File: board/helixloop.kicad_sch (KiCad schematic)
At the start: 2 parts, among them J1 Conn_01x04, J2 Conn_01x02

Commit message: finally get pixels all aligned right by laying out the sine-wave in chunks and using different pixel spacing for outer vs inner curve
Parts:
- added C1, C2: 10uF, Capacitor_SMD:C_0402_1005Metric, symbol Device:C
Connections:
- net +5V: now also C1.2, C2.2
- net GND: now also C1.1, C2.1
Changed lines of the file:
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@@
   (junction (at 116.205 48.895) (diameter 0) (color 0 0 0 0)
   )
+  (junction (at 154.305 37.465) (diameter 0) (color 0 0 0 0)
+  )
   (junction (at 154.305 29.21) (diameter 0) (color 0 0 0 0)
   )
   (junction (at 90.17 48.895) (diameter 0) (color 0 0 0 0)
   )
+  (junction (at 50.165 34.925) (diameter 0) (color 0 0 0 0)
+  )
+  (junction (at 57.785 42.545) (diameter 0) (color 0 0 0 0)
+  )
   (junction (at 154.305 48.895) (diameter 0) (color 0 0 0 0)
   )
@@
   )
   (junction (at 62.865 42.545) (diameter 0) (color 0 0 0 0)
+  )
+  (junction (at 154.305 40.005) (diameter 0) (color 0 0 0 0)
   )
   (no_connect (at 141.605 37.465))
   (no_connect (at 141.605 40.005))
-  (wire (pts (xy 45.72 42.545) (xy 62.865 42.545))
+  (wire (pts (xy 45.72 42.545) (xy 57.785 42.545))
     (stroke (width 0) (type default) (color 0 0 0 0))
   )
@@
     (stroke (width 0) (type default) (color 0 0 0 0))
   )
+  (wire (pts (xy 153.035 40.005) (xy 153.035 42.545))
+    (stroke (width 0) (type default) (color 0 0 0 0))
+  )
   (wire (pts (xy 140.335 37.465) (xy 141.605 37.465))
     (stroke (width 0) (type default) (color 0 0 0 0))
   )
+  (wire (pts (xy 57.785 42.545) (xy 62.865 42.545))
+    (stroke (width 0) (type default) (color 0 0 0 0))
+  )
   (wire (pts (xy 45.72 37.465) (xy 66.04 37.465))
     (stroke (width 0) (type default) (color 0 0 0 0))
@@
     (stroke (width 0) (type default) (color 0 0 0 0))
   )
+  (wire (pts (xy 153.035 37.465) (xy 153.035 34.925))
+    (stroke (width 0) (type default) (color 0 0 0 0))
+  )
   (wire (pts (xy 90.17 42.545) (xy 92.075 42.545))
     (stroke (width 0) (type default) (color 0 0 0 0))
@@
     (stroke (width 0) (type default) (color 0 0 0 0))
   )
+  (wire (pts (xy 153.035 34.925) (xy 149.225 34.925))
+    (stroke (width 0) (type default) (color 0 0 0 0))
+  )
+  (wire (pts (xy 153.035 42.545) (xy 149.225 42.545))
+    (stroke (width 0) (type default) (color 0 0 0 0))
+  )
   (wire (pts (xy 90.17 29.21) (xy 90.17 34.925))
     (stroke (width 0) (type default) (color 0 0 0 0))
@@
     (stroke (width 0) (type default) (color 0 0 0 0))
   )
-  (wire (pts (xy 45.72 34.925) (xy 62.865 34.925))
+  (wire (pts (xy 45.72 34.925) (xy 50.165 34.925))
     (stroke (width 0) (type default) (color 0 0 0 0))
   )
@@
     (stroke (width 0) (type default) (color 0 0 0 0))
   )
+  (wire (pts (xy 50.165 34.925) (xy 62.865 34.925))
+    (stroke (width 0) (type default) (color 0 0 0 0))
+  )
   (wire (pts (xy 116.205 29.21) (xy 154.305 29.21))
     (stroke (width 0) (type default) (color 0 0 0 0))
   )
+  (wire (pts (xy 154.305 40.005) (xy 153.035 40.005))
+    (stroke (width 0) (type default) (color 0 0 0 0))
+  )
+  (wire (pts (xy 50.165 30.48) (xy 50.165 34.925))
+    (stroke (width 0) (type default) (color 0 0 0 0))
+  )
+  (wire (pts (xy 57.785 30.48) (xy 57.785 42.545))
+    (stroke (width 0) (type default) (color 0 0 0 0))
+  )
   (wire (pts (xy 88.265 40.005) (xy 92.075 40.005))
+    (stroke (width 0) (type default) (color 0 0 0 0))
+  )
+  (wire (pts (xy 154.305 37.465) (xy 153.035 37.465))
     (stroke (width 0) (type default) (color 0 0 0 0))
   )
@@
     )
     (pin "1")
+  )
+  (symbol (lib_id "Device:C") (at 53.975 30.48 90) (unit 1)
+    (in_bom yes) (on_board yes) (fields_autoplaced)
+    (property "Reference" "C1" (id 0) (at 53.975 24.6212 90))
+    (property "Value" "10uF" (id 1) (at 53.975 27.1581 90))
+    (property "Footprint" "Capacitor_SMD:C_0402_1005Metric" (id 2) (at 57.785 29.5148 0)
+      (effects (font (size 1.27 1.27)) hide)
+    )
+    (property "Datasheet" "~" (id 3) (at 53.975 30.48 0)
+      (effects (font (size 1.27 1.27)) hide)
+    )
+    (pin "1")
+    (pin "2")
+  )
+  (symbol (lib_id "Device:C") (at 149.225 38.735 0) (unit 1)
+    (in_bom yes) (on_board yes)
+    (property "Reference" "C2" (id 0) (at 147.955 33.02 0)
+      (effects (font (size 1.27 1.27)) (justify left))
+    )
+    (property "Value" "10uF" (id 1) (at 146.685 44.45 0)
+      (effects (font (size 1.27 1.27)) (justify left))
+    )
+    (property "Footprint" "Capacitor_SMD:C_0402_1005Metric" (id 2) (at 150.1902 42.545 0)
+      (effects (font (size 1.27 1.27)) hide)
+    )
+    (property "Datasheet" "~" (id 3) (at 149.225 38.735 0)
+      (effects (font (size 1.27 1.27)) hide)
+    )
+    (pin "1")
+    (pin "2")
   )
   (symbol (lib_id "power:+5V") (at 154.305 48.895 180) (unit 1)
@@
       (reference "#PWR0110") (unit 1) (value "+5V") (footprint "")
     )
+    (path "/be7e036f-0d5d-4156-a7b8-31f688740589"
+      (reference "C1") (unit 1) (value "10uF") (footprint "Capacitor_SMD:C_0402_1005Metric")
+    )
+    (path "/cb59f15f-90e9-4305-b7cf-ed2b3c2ebbf8"
+      (reference "C2") (unit 1) (value "10uF") (footprint "Capacitor_SMD:C_0402_1005Metric")
+    )
     (path "/b7ef0c2d-d029-4ee4-8532-c6efa483cf4c/e5639c70-98d2-40ea-b831-829e12089cc3"

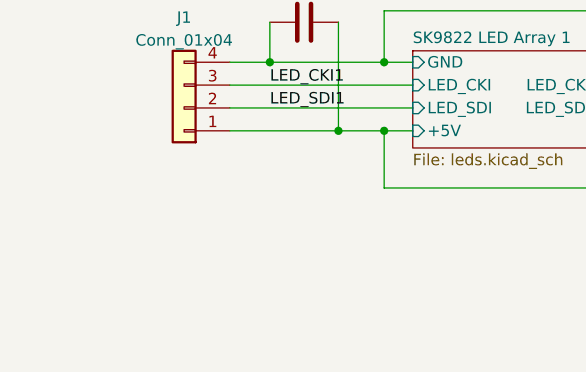
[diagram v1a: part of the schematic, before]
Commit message: add some labels to the back
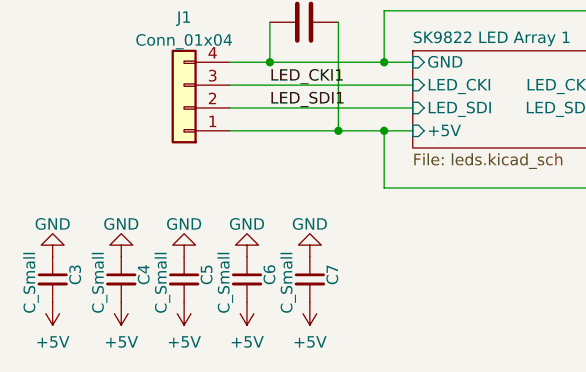
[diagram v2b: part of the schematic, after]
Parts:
- added C3, C4, C5, C6, C7: C_Small, Capacitor_SMD:C_0402_1005Metric, symbol Device:C_Small
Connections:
- net +5V: now also C3.2, C4.2, C5.2, C6.2, C7.2
- net GND: now also C3.1, C4.1, C5.1, C6.1, C7.1

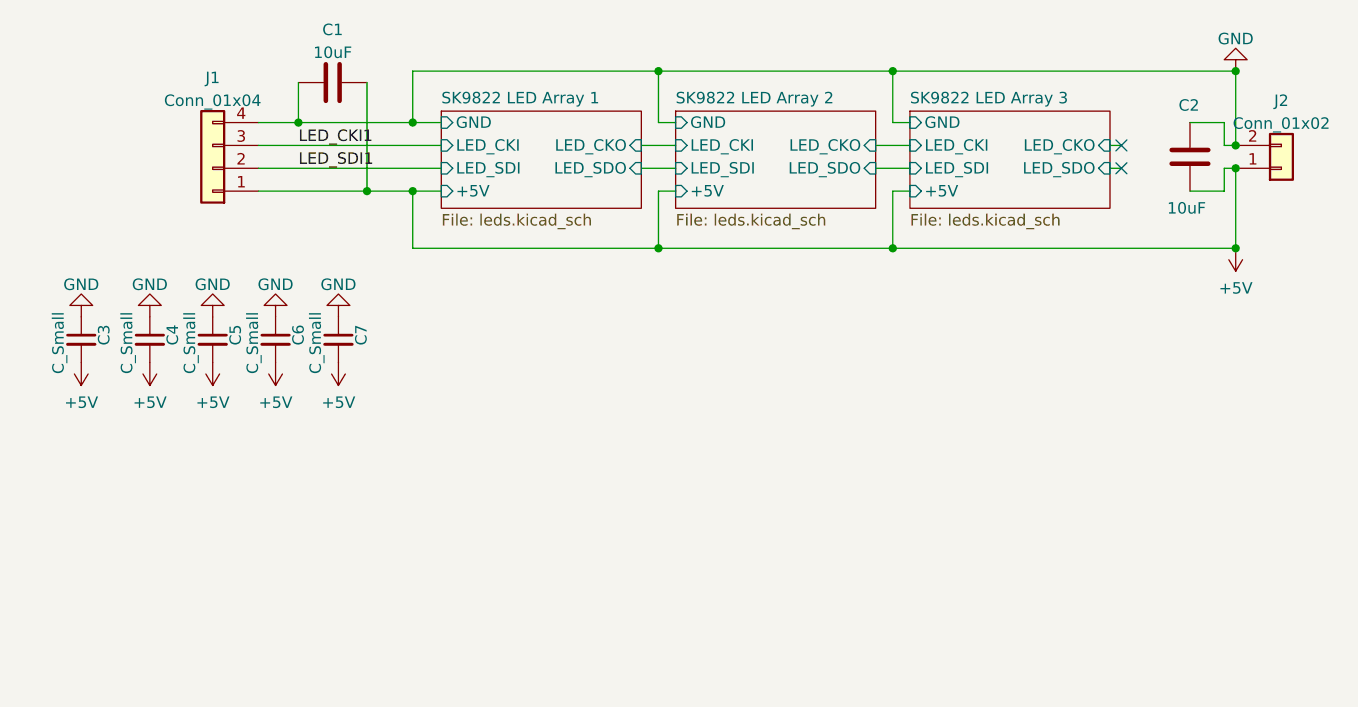
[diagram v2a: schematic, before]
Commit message: fix the SK9822-EC20 footprint, which wasn't to spec for some reason? sprinkle in capacitors in a more decorative arrangement; add a mounting hole in the center; fix all ERC errors
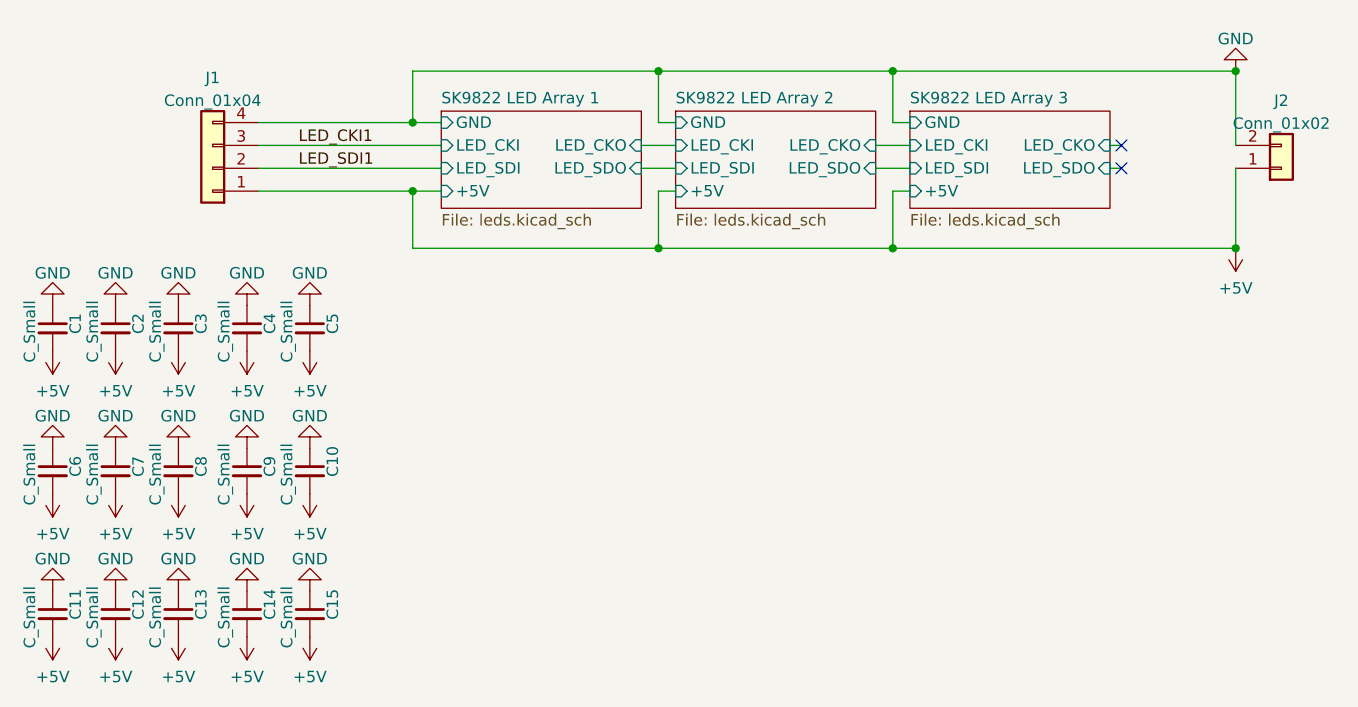
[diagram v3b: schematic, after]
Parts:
- removed C1, C2: 10uF, Capacitor_SMD:C_0402_1005Metric, symbol Device:C
- added C1, C10, C11, C12, C13, C14, C15, C2, C8, C9: C_Small, Capacitor_SMD:C_0402_1005Metric, symbol Device:C_Small
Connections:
- net +5V: now also C1.2, C10.2, C11.2, C12.2, C13.2, C14.2, C15.2, C2.2, C8.2, C9.2
- net GND: now also C1.1, C10.1, C11.1, C12.1, C13.1, C14.1, C15.1, C2.1, C8.1, C9.1
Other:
- moved on the sheet: C3, C4, C5

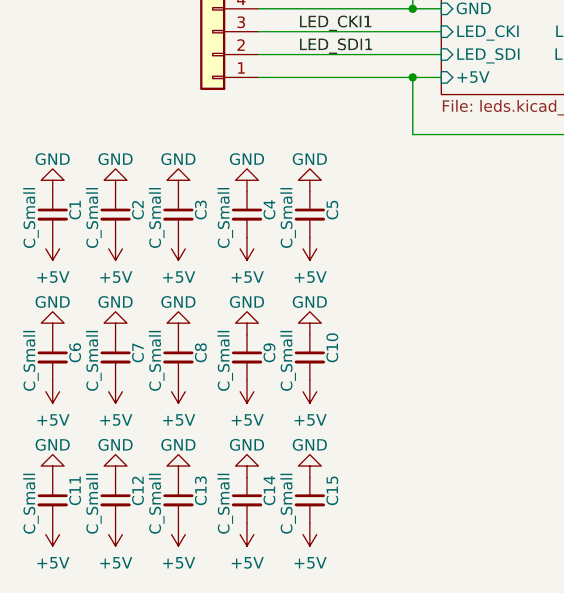
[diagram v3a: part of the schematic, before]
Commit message: annotate capacitors as 10uF
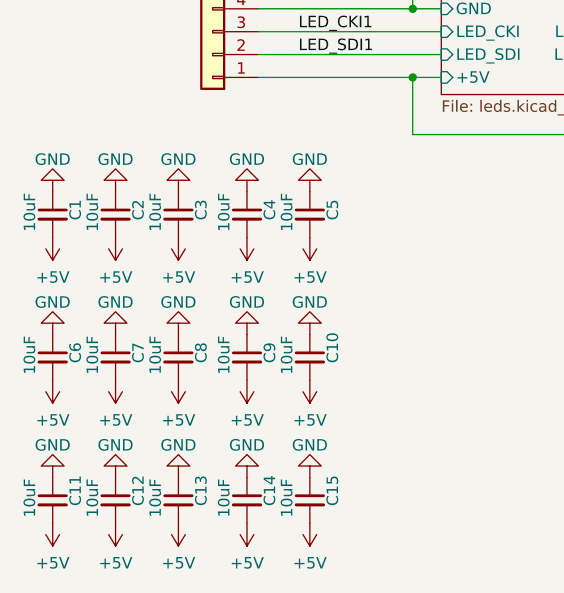
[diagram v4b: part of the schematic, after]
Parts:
- C1, C10, C11, C12, C13, C14, C15, C2, C3, C4, C5, C6, C7, C8, C9: value C_Small -> 10uF
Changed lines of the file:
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@@
       (effects (font (size 1.27 1.27)) (justify left))
     )
-    (property "Value" "C_Small" (id 1) (at 41.91 61.595 90)
+    (property "Value" "10uF" (id 1) (at 41.91 59.69 90)
       (effects (font (size 1.27 1.27)) (justify left))
     )
@@
       (effects (font (size 1.27 1.27)) (justify left))
     )
-    (property "Value" "C_Small" (id 1) (at 48.895 77.47 90)
+    (property "Value" "10uF" (id 1) (at 48.895 75.565 90)
       (effects (font (size 1.27 1.27)) (justify left))
     )
@@
       (effects (font (size 1.27 1.27)) (justify left))
     )
-    (property "Value" "C_Small" (id 1) (at 34.29 77.47 90)
+    (property "Value" "10uF" (id 1) (at 34.29 75.565 90)
       (effects (font (size 1.27 1.27)) (justify left))
     )
@@
       (effects (font (size 1.27 1.27)) (justify left))
     )
-    (property "Value" "C_Small" (id 1) (at 27.305 93.345 90)
+    (property "Value" "10uF" (id 1) (at 27.305 91.44 90)
       (effects (font (size 1.27 1.27)) (justify left))
     )
@@
       (effects (font (size 1.27 1.27)) (justify left))
     )
-    (property "Value" "C_Small" (id 1) (at 48.895 61.595 90)
+    (property "Value" "10uF" (id 1) (at 48.895 59.69 90)
       (effects (font (size 1.27 1.27)) (justify left))
     )
@@
       (effects (font (size 1.27 1.27)) (justify left))
     )
-    (property "Value" "C_Small" (id 1) (at 34.29 93.345 90)
+    (property "Value" "10uF" (id 1) (at 34.29 91.44 90)
       (effects (font (size 1.27 1.27)) (justify left))
     )
@@
       (effects (font (size 1.27 1.27)) (justify left))
     )
-    (property "Value" "C_Small" (id 1) (at 34.29 61.595 90)
+    (property "Value" "10uF" (id 1) (at 34.29 59.69 90)
       (effects (font (size 1.27 1.27)) (justify left))
     )
@@
       (effects (font (size 1.27 1.27)) (justify left))
     )
-    (property "Value" "C_Small" (id 1) (at 41.91 77.47 90)
+    (property "Value" "10uF" (id 1) (at 41.91 75.565 90)
       (effects (font (size 1.27 1.27)) (justify left))
     )
@@
       (effects (font (size 1.27 1.27)) (justify left))
     )
-    (property "Value" "C_Small" (id 1) (at 20.32 61.595 90)
+    (property "Value" "10uF" (id 1) (at 20.32 59.69 90)
       (effects (font (size 1.27 1.27)) (justify left))
     )
@@
       (effects (font (size 1.27 1.27)) (justify left))
     )
-    (property "Value" "C_Small" (id 1) (at 41.91 93.345 90)
+    (property "Value" "10uF" (id 1) (at 41.91 91.44 90)
       (effects (font (size 1.27 1.27)) (justify left))
     )
@@
       (effects (font (size 1.27 1.27)) (justify left))
     )
-    (property "Value" "C_Small" (id 1) (at 20.32 93.345 90)
+    (property "Value" "10uF" (id 1) (at 20.32 91.44 90)
       (effects (font (size 1.27 1.27)) (justify left))
     )
@@
       (effects (font (size 1.27 1.27)) (justify left))
     )
-    (property "Value" "C_Small" (id 1) (at 27.305 61.595 90)
+    (property "Value" "10uF" (id 1) (at 27.305 59.69 90)
       (effects (font (size 1.27 1.27)) (justify left))
     )
@@
       (effects (font (size 1.27 1.27)) (justify left))
     )
-    (property "Value" "C_Small" (id 1) (at 27.305 77.47 90)
+    (property "Value" "10uF" (id 1) (at 27.305 75.565 90)
       (effects (font (size 1.27 1.27)) (justify left))
     )
@@
       (effects (font (size 1.27 1.27)) (justify left))
     )
-    (property "Value" "C_Small" (id 1) (at 48.895 93.345 90)
+    (property "Value" "10uF" (id 1) (at 48.895 91.44 90)
       (effects (font (size 1.27 1.27)) (justify left))
     )
@@
       (effects (font (size 1.27 1.27)) (justify left))
     )
-    (property "Value" "C_Small" (id 1) (at 20.32 77.47 90)
+    (property "Value" "10uF" (id 1) (at 20.32 75.565 90)
       (effects (font (size 1.27 1.27)) (justify left))
     )
@@
     )
     (path "/6ff76503-41d7-4796-a7b5-0bbc2358828a"
-      (reference "C1") (unit 1) (value "C_Small") (footprint "Capacitor_SMD:C_0402_1005Metric")
+      (reference "C1") (unit 1) (value "10uF") (footprint "Capacitor_SMD:C_0402_1005Metric")
     )
     (path "/cd208a04-31a4-4b07-a1da-06aa8a3d5395"
-      (reference "C2") (unit 1) (value "C_Small") (footprint "Capacitor_SMD:C_0402_1005Metric")
+      (reference "C2") (unit 1) (value "10uF") (footprint "Capacitor_SMD:C_0402_1005Metric")
     )
     (path "/6456da73-1a9e-4e58-8070-8258976e80d7"
-      (reference "C3") (unit 1) (value "C_Small") (footprint "Capacitor_SMD:C_0402_1005Metric")
+      (reference "C3") (unit 1) (value "10uF") (footprint "Capacitor_SMD:C_0402_1005Metric")
     )
     (path "/113bd2cd-3065-4ee5-92fe-14e6a9af2720"
-      (reference "C4") (unit 1) (value "C_Small") (footprint "Capacitor_SMD:C_0402_1005Metric")
+      (reference "C4") (unit 1) (value "10uF") (footprint "Capacitor_SMD:C_0402_1005Metric")
     )
     (path "/433e3d54-e3ba-430a-90e1-0158cd908b2b"
-      (reference "C5") (unit 1) (value "C_Small") (footprint "Capacitor_SMD:C_0402_1005Metric")
+      (reference "C5") (unit 1) (value "10uF") (footprint "Capacitor_SMD:C_0402_1005Metric")
     )
     (path "/f2350876-4a35-419f-98ea-61961d04d925"
-      (reference "C6") (unit 1) (value "C_Small") (footprint "Capacitor_SMD:C_0402_1005Metric")
+      (reference "C6") (unit 1) (value "10uF") (footprint "Capacitor_SMD:C_0402_1005Metric")
     )
     (path "/db32baab-9840-4108-93a8-24c6a75773ca"
-      (reference "C7") (unit 1) (value "C_Small") (footprint "Capacitor_SMD:C_0402_1005Metric")
+      (reference "C7") (unit 1) (value "10uF") (footprint "Capacitor_SMD:C_0402_1005Metric")
     )
     (path "/2ce0f34b-dfa9-4e3c-bb5d-4d20320db7d9"
-      (reference "C8") (unit 1) (value "C_Small") (footprint "Capacitor_SMD:C_0402_1005Metric")
+      (reference "C8") (unit 1) (value "10uF") (footprint "Capacitor_SMD:C_0402_1005Metric")
     )
     (path "/6f8b0590-8bc6-488c-b4bb-d261c8e4a275"
-      (reference "C9") (unit 1) (value "C_Small") (footprint "Capacitor_SMD:C_0402_1005Metric")
+      (reference "C9") (unit 1) (value "10uF") (footprint "Capacitor_SMD:C_0402_1005Metric")
     )
     (path "/1541eae3-0981-45bb-ab2c-18ebd491fa8a"
-      (reference "C10") (unit 1) (value "C_Small") (footprint "Capacitor_SMD:C_0402_1005Metric")
+      (reference "C10") (unit 1) (value "10uF") (footprint "Capacitor_SMD:C_0402_1005Metric")
     )
     (path "/77c80b6d-d8c2-4a32-9849-9dcbab3105a8"
-      (reference "C11") (unit 1) (value "C_Small") (footprint "Capacitor_SMD:C_0402_1005Metric")
+      (reference "C11") (unit 1) (value "10uF") (footprint "Capacitor_SMD:C_0402_1005Metric")
     )
     (path "/30e5487b-95d6-47e7-b90d-4fac95ff8029"
-      (reference "C12") (unit 1) (value "C_Small") (footprint "Capacitor_SMD:C_0402_1005Metric")
+      (reference "C12") (unit 1) (value "10uF") (footprint "Capacitor_SMD:C_0402_1005Metric")
     )
     (path "/60a68684-7ecc-4f11-bde6-d41cf56ae4af"
-      (reference "C13") (unit 1) (value "C_Small") (footprint "Capacitor_SMD:C_0402_1005Metric")
+      (reference "C13") (unit 1) (value "10uF") (footprint "Capacitor_SMD:C_0402_1005Metric")
     )
     (path "/759000a9-b227-499c-be4f-b2642d7ebf11"
-      (reference "C14") (unit 1) (value "C_Small") (footprint "Capacitor_SMD:C_0402_1005Metric")
+      (reference "C14") (unit 1) (value "10uF") (footprint "Capacitor_SMD:C_0402_1005Metric")
     )
     (path "/e16e2149-6378-46bf-9ad4-07cb55fb2362"
-      (reference "C15") (unit 1) (value "C_Small") (footprint "Capacitor_SMD:C_0402_1005Metric")
+      (reference "C15") (unit 1) (value "10uF") (footprint "Capacitor_SMD:C_0402_1005Metric")
     )
     (path "/b7ef0c2d-d029-4ee4-8532-c6efa483cf4c/e5639c70-98d2-40ea-b831-829e12089cc3"
